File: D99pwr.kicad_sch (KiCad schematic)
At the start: 40 parts, among them IC1 TPS560430YFQDBVRQ1, IC2 NCP730BMT1500TBG, Q3B BC847BDW1, U2 MAX40203AUK, U3 MCP1640BCH, U4 MAX40203AUK

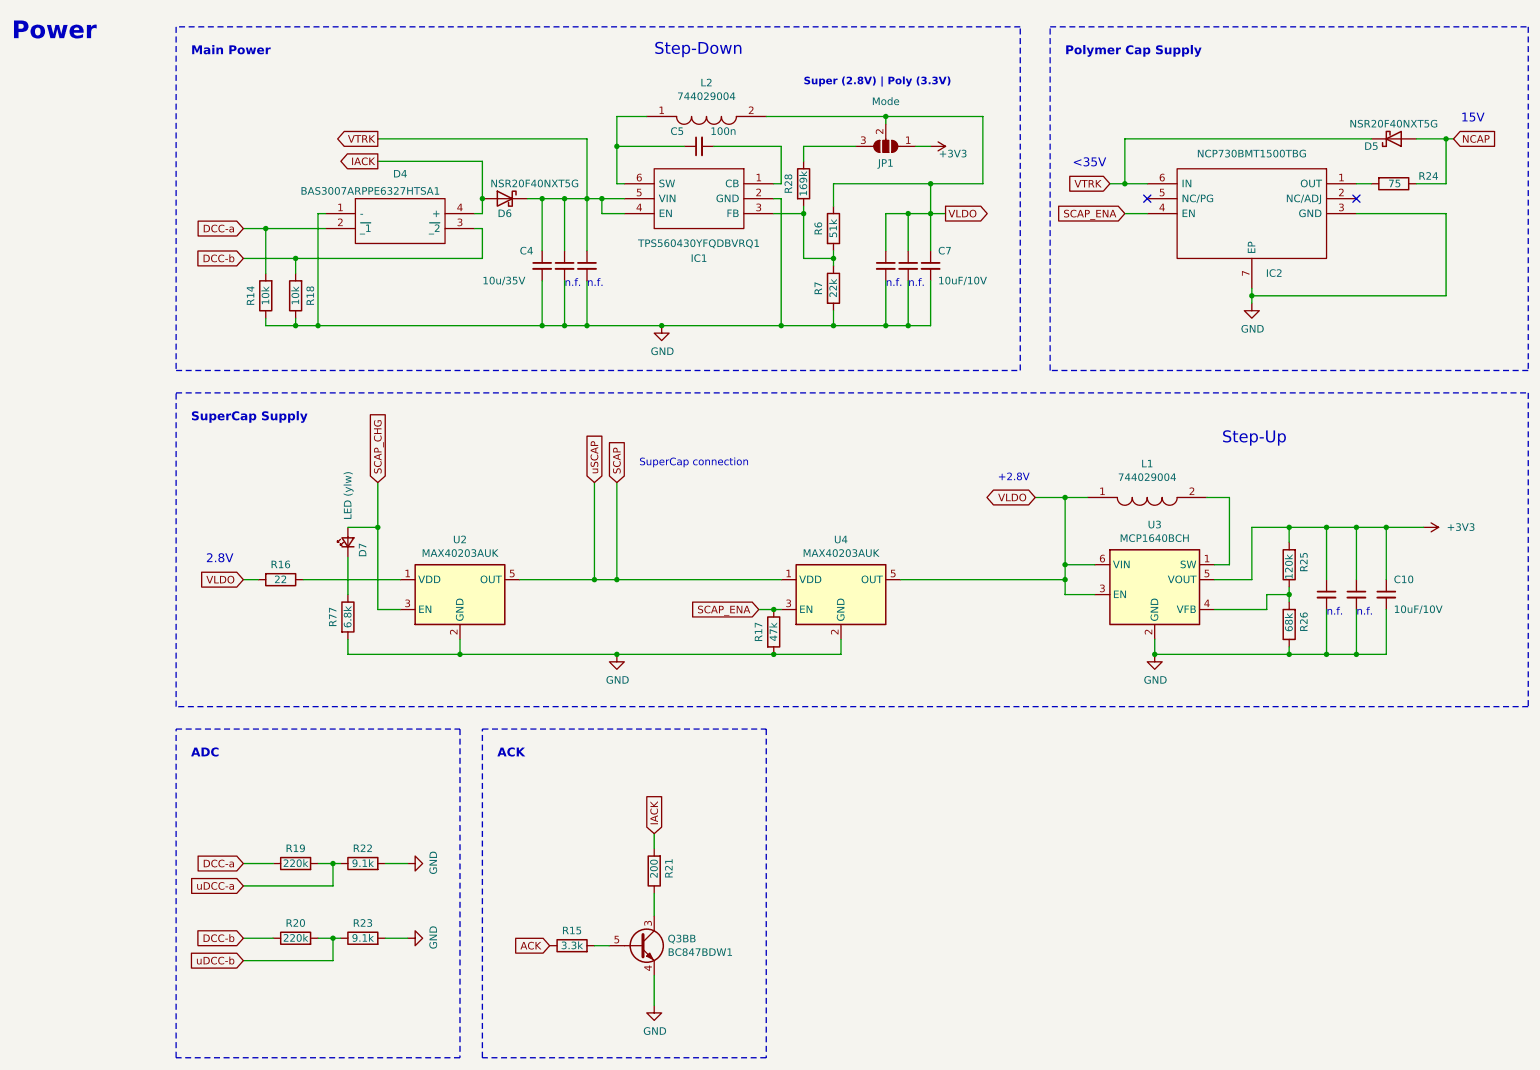
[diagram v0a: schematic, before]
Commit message: mod: ncap leakage resistor
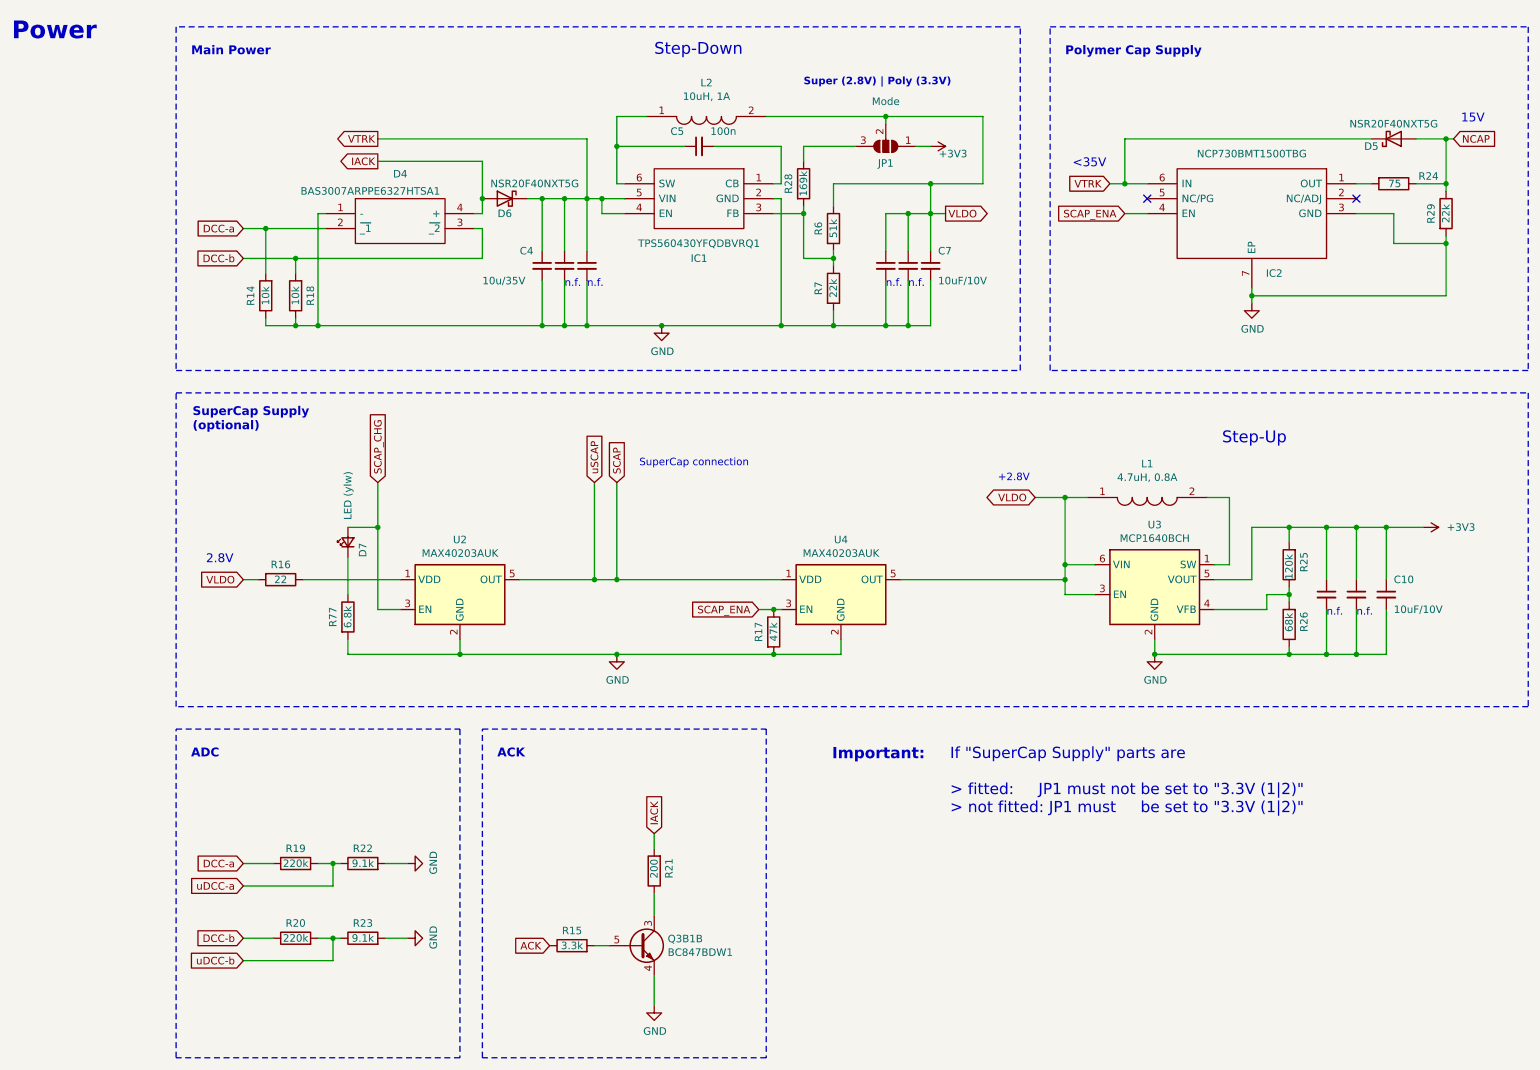
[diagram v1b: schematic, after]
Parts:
- added R29: 22k, Resistor_SMD:R_0402_1005Metric, symbol Device:R
- D5, D6: footprint Diode_SMD:D_0603_1608Metric -> RTB:NSR20F40NXT5G
- L1: value 744029004 -> 4.7uH, 0.8A
- L2: value 744029004 -> 10uH, 1A; JLCPCB C2649333 -> C2045611
- renumbered Q3B to Q3B1
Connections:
- net GND: now also R29.2
- net NCAP: now also R29.1
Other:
- note added: "If "SuperCap Supply" parts are > fitted: JP1 must not be set to "3.3V (1|2)" > not fitted: JP1 must be set to "3.3V (1|2)""
- note added: "Important:"
- note added: "SuperCap Supply (optional)"
- note removed: "SuperCap Supply"
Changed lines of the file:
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@@
 		)
 	)
+	(text "If \"SuperCap Supply\" parts are\n\n> fitted:     JP1 must not be set to \"3.3V (1|2)\"\n> not fitted: JP1 must     be set to \"3.3V (1|2)\""
+		(exclude_from_sim no)
+		(at 176.022 144.78 0)
+		(effects
+			(font
+				(size 1.905 1.905)
+				(thickness 0.2381)
+				(color 0 0 0 1)
+			)
+			(justify left)
+		)
+	)
 	(text "n.f."
 		(exclude_from_sim no)
@@
 		)
 	)
-	(text "SuperCap Supply"
+	(text "SuperCap Supply\n(optional)"
 		(exclude_from_sim no)
-		(at 46.99 83.82 0)
+		(at 47.244 85.344 0)
 		(effects
 			(font
@@
 		)
 	)
+	(text "Important:"
+		(exclude_from_sim no)
+		(at 155.956 140.208 0)
+		(effects
+			(font
+				(size 1.905 1.905)
+				(thickness 0.381)
+				(bold yes)
+				(color 194 0 194 1)
+			)
+			(justify left)
+		)
+	)
 	(text "15V"
 		(exclude_from_sim no)
@@
 	)
 	(junction
+		(at 260.35 53.34)
+		(diameter 0)
+		(color 0 0 0 0)
+	)
+	(junction
 		(at 233.68 101.6)
 		(diameter 0)
@@
 	)
 	(junction
+		(at 260.35 43.18)
+		(diameter 0)
+		(color 0 0 0 0)
+	)
+	(junction
 		(at 64.77 67.31)
 		(diameter 0)
@@
 	(wire
 		(pts
+			(xy 260.35 52.07) (xy 260.35 53.34)
+		)
+		(stroke
+			(width 0)
+			(type default)
+		)
+	)
+	(wire
+		(pts
 			(xy 106.68 54.61) (xy 106.68 45.72)
 		)
@@
 	(wire
 		(pts
-			(xy 260.35 48.26) (xy 260.35 62.23)
+			(xy 260.35 53.34) (xy 260.35 62.23)
 		)
 		(stroke
@@
 	(wire
 		(pts
+			(xy 251.46 48.26) (xy 245.11 48.26)
+		)
+		(stroke
+			(width 0)
+			(type default)
+		)
+	)
+	(wire
+		(pts
 			(xy 260.35 35.56) (xy 261.62 35.56)
 		)
@@
 	(wire
 		(pts
+			(xy 251.46 53.34) (xy 251.46 48.26)
+		)
+		(stroke
+			(width 0)
+			(type default)
+		)
+	)
+	(wire
+		(pts
 			(xy 78.74 101.6) (xy 78.74 93.98)
 		)
@@
 	(wire
 		(pts
-			(xy 245.11 48.26) (xy 260.35 48.26)
+			(xy 251.46 53.34) (xy 260.35 53.34)
 		)
 		(stroke
@@
 	(wire
 		(pts
+			(xy 260.35 43.18) (xy 260.35 44.45)
+		)
+		(stroke
+			(width 0)
+			(type default)
+		)
+	)
+	(wire
+		(pts
 			(xy 156.21 43.18) (xy 172.72 43.18)
 		)
@@
 		(on_board yes)
 		(dnp no)
-		(property "Reference" "Q3B"
+		(property "Reference" "Q3B1"
 			(at 128.016 171.5516 0)
 			(effects
@@
 			(project "D99"
 				(path "/df79ce8b-a870-46f6-824c-d442122538ae/00000000-0000-0000-0000-00005ca7768a"
-					(reference "Q3B")
+					(reference "Q3B1")
 					(unit 2)
 				)
@@
 			)
 		)
-		(property "Footprint" "Diode_SMD:D_0603_1608Metric"
+		(property "Footprint" "RTB:NSR20F40NXT5G"
 			(at 100.33 45.72 0)
 			(effects
@@
 			)
 		)
-		(property "Footprint" "Diode_SMD:D_0603_1608Metric"
+		(property "Footprint" "RTB:NSR20F40NXT5G"
 			(at 251.46 35.56 0)
 			(effects
@@
 			)
 		)
-		(property "Value" "744029004"
+		(property "Value" "4.7uH, 0.8A"
 			(at 209.55 93.1164 0)
 			(effects
@@
 			)
 		)
-		(property "Value" "744029004"
+		(property "Value" "10uH, 1A"
 			(at 134.62 28.3464 0)
 			(effects
@@
 			)
 		)
-		(property "Datasheet" "http://componentsearchengine.com/Datasheets/1/744029004.pdf"
+		(property "Datasheet" "http://componentsearchengine.com/Datasheets/1/744025100.pdf"
 			(at 140.97 33.02 0)
 			(effects
@@
 			)
 		)
-		(property "Description" "170mΩ 4.7uH 800mA 800mA ±30% SMD,2.8x2.8mm Power Inductors ROHS"
+		(property "Description" "1.1A 10uH 190mΩ 1A ±20% 2828 Power Inductors ROHS"
 			(at 140.97 35.56 0)
 			(effects
@@
 			)
 		)
-		(property "JLCPCB" "C2649333"
+		(property "JLCPCB" "C2045611"
 			(at 124.46 31.75 0)
 			(effects
@@
 					(unit 1)
 				)
+			)
+		)
+	)
+	(symbol
+		(lib_id "Device:R")
+		(at 260.35 48.26 0)
+		(unit 1)
+		(exclude_from_sim no)
+		(in_bom yes)
+		(on_board yes)
+		(dnp no)
+		(property "Reference" "R29"
+			(at 257.81 48.26 90)
+			(effects
+				(font
+					(size 1.27 1.27)
+				)
+			)
+		)
+		(property "Value" "22k"
+			(at 260.35 48.26 90)
+			(effects
+				(font
+					(size 1.27 1.27)
+				)
+			)
+		)
+		(property "Footprint" "Resistor_SMD:R_0402_1005Metric"
+			(at 258.572 48.26 90)
+			(effects
+				(font
+					(size 1.27 1.27)
+				)
+				(hide yes)
+			)
+		)
+		(property "Datasheet" "~"
+			(at 260.35 48.26 0)
+			(effects
+				(font
+					(size 1.27 1.27)
+				)
+				(hide yes)
+			)
+		)
+		(property "Description" ""
+			(at 260.35 48.26 90)
+			(effects
+				(font
+					(size 1.27 1.27)
+				)
+				(hide yes)
+			)
+		)
+		(property "JLCPCB" ""
+			(at 260.35 48.26 90)
+			(effects
+				(font
+					(size 1.27 1.27)
+				)
+				(hide yes)
+			)
+		)
+		(pin "1"
+		)
+		(pin "2"
+		)
+		(instances
+			(project "D99"
+				(path "/df79ce8b-a870-46f6-824c-d442122538ae/00000000-0000-0000-0000-00005ca7768a"
+					(reference "R29")
+					(unit 1)
+				)

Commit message: mod: refactoring
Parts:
- C10, C11, C6, C7, C8, C9: JLCPCB C19702 -> (none); LCSC Part # (none) -> C19702
- C12, C13, C4: JLCPCB C194427 -> (none); LCSC Part # (none) -> C194427
- C5: JLCPCB C307331 -> (none); LCSC Part # (none) -> C307331
- D4: JLCPCB C6430958 -> (none); LCSC Part # (none) -> C6430958
- D5, D6: JLCPCB C153761 -> (none); LCSC Part # (none) -> C153761
- IC1: JLCPCB C1849549 -> (none); LCSC Part # (none) -> C1849549
- IC2: JLCPCB C892817 -> (none); LCSC Part # (none) -> C892817
- L1: JLCPCB C2649333 -> (none); LCSC Part # (none) -> C2649333
- L2: JLCPCB C2045611 -> (none); LCSC Part # (none) -> C2045611
- Q3B1: JLCPCB C82368 -> (none); LCSC Part # (none) -> C82368
- R14, R18: JLCPCB C25744 -> (none); LCSC Part # (none) -> C25744
- R15: JLCPCB C25890 -> (none); LCSC Part # (none) -> C25890
- R16: JLCPCB C25092 -> (none); LCSC Part # (none) -> C25092
- R17: JLCPCB C25792 -> (none); LCSC Part # (none) -> C25792
- R19, R20: JLCPCB C25767 -> (none); LCSC Part # (none) -> C25767
- R21: JLCPCB C8218 -> (none); LCSC Part # (none) -> C8218
- R22, R23: JLCPCB C25926 -> (none); LCSC Part # (none) -> C25926
- R24: JLCPCB C4275 -> (none); LCSC Part # (none) -> C4275
- R25: JLCPCB C25750 -> (none); LCSC Part # (none) -> C25750
- R26: JLCPCB C36871 -> (none); LCSC Part # (none) -> C36871
- R28: JLCPCB C25758 -> (none); LCSC Part # (none) -> C25758
- R29: LCSC Part # (none) -> C25768
- R6: JLCPCB C25794 -> (none); LCSC Part # (none) -> C25794
- R7: JLCPCB C25768 -> (none); LCSC Part # (none) -> C25768
- R77: JLCPCB C23212 -> (none); LCSC Part # (none) -> C23212
- U2: LCSC Part # (none) -> C2653639
- U3: JLCPCB C478087 -> (none); LCSC Part # (none) -> C478087
- U4: JLCPCB C2653639 -> (none); LCSC Part # (none) -> C2653639
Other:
- note added: "3.3V: R25 = 120 Ohm 5.1V: R25 = 220 Ohm Use 1% Resistors for R25,R26"
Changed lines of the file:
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@@
 		)
 	)
+	(text "3.3V: R25 = 120 Ohm\n5.1V: R25 = 220 Ohm\nUse 1% Resistors for R25,R26"
+		(exclude_from_sim no)
+		(at 228.092 95.25 0)
+		(effects
+			(font
+				(size 1.27 1.27)
+			)
+			(justify left)
+		)
+	)
 	(text "Main Power"
 		(exclude_from_sim no)
@@
 			)
 		)
-		(property "JLCPCB" "C19702"
+		(property "LCSC Part #" "C19702"
 			(at 245.11 113.03 0)
 			(effects
@@
 			)
 		)
-		(property "JLCPCB" "C8218"
+		(property "LCSC Part #" "C8218"
 			(at 125.73 160.02 90)
 			(effects
@@
 			)
 		)
-		(property "JLCPCB" "C25890"
+		(property "LCSC Part #" "C25890"
 			(at 111.76 172.72 90)
 			(effects
@@
 			)
 		)
-		(property "JLCPCB" "C19702"
+		(property "LCSC Part #" "C19702"
 			(at 172.72 57.15 0)
 			(effects
@@
 			)
 		)
-		(property "JLCPCB" "C82368"
+		(property "LCSC Part #" "C82368"
 			(at 123.19 172.72 0)
 			(effects
@@
 			)
 		)
-		(property "JLCPCB" "C25767"
+		(property "LCSC Part #" "C25767"
 			(at 64.77 158.75 90)
 			(effects
@@
 			)
 		)
-		(property "JLCPCB" "C25926"
+		(property "LCSC Part #" "C25926"
 			(at 76.2 158.75 90)
 			(effects
@@
 			)
 		)
-		(property "JLCPCB" "C25767"
+		(property "LCSC Part #" "C25767"
 			(at 64.77 171.45 90)
 			(effects
@@
 			)
 		)
-		(property "JLCPCB" "C25926"
+		(property "LCSC Part #" "C25926"
 			(at 76.2 171.45 90)
 			(effects
@@
 			)
 		)
-		(property "JLCPCB" "C2653639"
+		(property "LCSC Part #" "C2653639"
 			(at 157.48 113.03 0)
 			(effects
@@
 			)
 		)
-		(property "JLCPCB" "C25750"
+		(property "LCSC Part #" "C25750"
 			(at 233.68 107.95 90)
 			(effects
@@
 			)
 		)
-		(property "JLCPCB" "C36871"
+		(property "LCSC Part #" "C36871"
 			(at 233.68 118.11 90)
 			(effects
@@
 			)
 		)
-		(property "JLCPCB" "C25744"
+		(property "LCSC Part #" "C25744"
 			(at 64.77 62.23 90)
 			(effects
@@
 			)
 		)
-		(property "JLCPCB" "C478087"
+		(property "LCSC Part #" "C478087"
 			(at 210.82 113.03 0)
 			(effects
@@
 			)
 		)
-		(property "JLCPCB" "C23212"
+		(property "LCSC Part #" "C23212"
 			(at 73.66 116.84 90)
 			(effects
@@
 			)
 		)
-		(property "JLCPCB" "C25744"
+		(property "LCSC Part #" "C25744"
 			(at 59.69 62.23 90)
 			(effects
@@
 			)
 		)
-		(property "JLCPCB" "C194427"
+		(property "LCSC Part #" "C194427"
 			(at 106.68 57.15 0)
 			(effects
@@
 			)
 		)
-		(property "JLCPCB" "C25092"
+		(property "LCSC Part #" "C25092"
 			(at 62.23 110.49 90)
 			(effects
@@
 			)
 		)
-		(property "JLCPCB" ""
+		(property "LCSC Part #" "C2653639"
 			(at 92.71 113.03 0)
 			(effects
@@
 			)
 		)
-		(property "JLCPCB" "C25792"
+		(property "LCSC Part #" "C25792"
 			(at 146.05 119.38 90)
 			(effects
@@
 			)
 		)
-		(property "JLCPCB" "C6430958"
+		(property "LCSC Part #" "C6430958"
 			(at 69.85 48.26 0)
 			(effects
@@
 			)
 		)
-		(property "JLCPCB" "C1849549"
+		(property "LCSC Part #" "C1849549"
 			(at 146.05 43.18 0)
 			(effects
@@
 			)
 		)
-		(property "JLCPCB" "C307331"
+		(property "LCSC Part #" "C307331"
 			(at 133.35 36.83 90)
 			(effects
@@
 			)
 		)
-		(property "JLCPCB" "C19702"
+		(property "LCSC Part #" "C19702"
 			(at 250.19 113.03 0)
 			(effects
@@
 			)
 		)
-		(property "JLCPCB" "C19702"
+		(property "LCSC Part #" "C19702"
 			(at 168.91 57.15 0)
 			(effects
@@
 			)
 		)
-		(property "JLCPCB" "C153761"
+		(property "LCSC Part #" "C153761"
 			(at 100.33 45.72 0)
 			(effects
@@
 			)
 		)
-		(property "JLCPCB" "C153761"
+		(property "LCSC Part #" "C153761"
 			(at 251.46 35.56 0)
 			(effects
@@
 			)
 		)
-		(property "JLCPCB" "C4275"
+		(property "LCSC Part #" "C4275"
 			(at 251.46 43.18 90)
 			(effects
@@
 			)
 		)
-		(property "JLCPCB" "C19702"
+		(property "LCSC Part #" "C19702"
 			(at 165.1 57.15 0)
 			(effects
@@
 			)
 		)
-		(property "JLCPCB" "C2649333"
+		(property "LCSC Part #" "C2649333"
 			(at 199.39 96.52 0)
 			(effects
@@
 			)
 		)
-		(property "JLCPCB" "C2045611"
+		(property "LCSC Part #" "C2045611"
 			(at 124.46 31.75 0)
 			(effects
@@
 			)
 		)
-		(property "JLCPCB" "C19702"
+		(property "LCSC Part #" "C19702"
 			(at 240.03 113.03 0)
 			(effects
@@
 			)
 		)
-		(property "JLCPCB" "C194427"
+		(property "LCSC Part #" "C194427"
 			(at 110.49 57.15 0)
 			(effects
@@
 			)
 		)
-		(property "JLCPCB" "C194427"
+		(property "LCSC Part #" "C194427"
 			(at 114.3 57.15 0)
 			(effects
@@
 			)
 		)
-		(property "JLCPCB" "C25794"
+		(property "LCSC Part #" "C25794"
 			(at 156.21 50.8 90)
 			(effects
@@
 			)
 		)
-		(property "JLCPCB" "C25768"
+		(property "LCSC Part #" "C25768"
 			(at 156.21 60.96 90)
 			(effects
@@
 			)
 		)
-		(property "JLCPCB" "C25758"
+		(property "LCSC Part #" "C25758"
 			(at 151.13 43.18 90)
 			(effects
@@
 			)
 		)
-		(property "JLCPCB" "C892817"
+		(property "LCSC Part #" "C892817"
 			(at 245.11 43.18 0)
 			(effects
@@
 			)
 		)
-		(property "Description" ""
+		(property "Description" "-55℃~+155℃ 22kΩ 50V 62.5mW Thick Film Resistor ±1% ±100ppm/℃ 0402 Chip Resistor - Surface Mount ROHS"
 			(at 260.35 48.26 90)
 			(effects
@@
 			)
 		)
-		(property "JLCPCB" ""
+		(property "LCSC Part #" "C25768"
 			(at 260.35 48.26 90)
 			(effects

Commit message: mod: refactoring
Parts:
- added unit 1 of Q3
- R21: value 200 -> 150; LCSC Part # C8218 -> C22808
- renumbered Q3B1 to Q3
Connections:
- no-connect marks 2 -> 5
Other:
- note added: "(or 5.0V)"
- note added: "3.3V: R25 = 120 Ohm 5.0V: R25 = 210 Ohm Use 1% Resistors for R25,R26"
- note removed: "3.3V: R25 = 120 Ohm 5.1V: R25 = 220 Ohm Use 1% Resistors for R25,R26"
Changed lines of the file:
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@@
 		)
 	)
+	(text "(or 5.0V)"
+		(exclude_from_sim no)
+		(at 264.668 104.394 0)
+		(effects
+			(font
+				(size 1.27 1.27)
+			)
+		)
+	)
 	(text "ACK"
 		(exclude_from_sim no)
@@
 		)
 	)
-	(text "3.3V: R25 = 120 Ohm\n5.1V: R25 = 220 Ohm\nUse 1% Resistors for R25,R26"
+	(text "3.3V: R25 = 120 Ohm\n5.0V: R25 = 210 Ohm\nUse 1% Resistors for R25,R26"
 		(exclude_from_sim no)
 		(at 228.092 95.25 0)
@@
 	)
 	(no_connect
+		(at 100.33 151.13)
+	)
+	(no_connect
+		(at 107.95 156.21)
+	)
+	(no_connect
 		(at 245.11 45.72)
 	)
+	(no_connect
+		(at 107.95 146.05)
+	)
 	(polyline
 		(pts
@@
 			)
 		)
-		(property "Value" "200"
+		(property "Value" "150"
 			(at 125.73 161.29 90)
 			(effects
@@
 			)
 		)
-		(property "Description" "-55℃~+155℃ 100mW 200Ω 75V Thick Film Resistor ±1% ±100ppm/℃ 0603 Chip Resistor - Surface Mount ROHS"
+		(property "Description" "-55℃~+155℃ 100mW 150Ω 75V Thick Film Resistor ±1% ±100ppm/℃ 0603 Chip Resistor - Surface Mount ROHS"
 			(at 125.73 160.02 90)
 			(effects
@@
 			)
 		)
-		(property "LCSC Part #" "C8218"
+		(property "LCSC Part #" "C22808"
 			(at 125.73 160.02 90)
 			(effects
@@
 		(on_board yes)
 		(dnp no)
-		(property "Reference" "Q3B1"
+		(property "Reference" "Q3"
 			(at 128.016 171.5516 0)
 			(effects
@@
 			(project "D99"
 				(path "/df79ce8b-a870-46f6-824c-d442122538ae/00000000-0000-0000-0000-00005ca7768a"
-					(reference "Q3B1")
+					(reference "Q3")
 					(unit 2)
 				)
@@
 					(unit 1)
 				)
+			)
+		)
+	)
+	(symbol
+		(lib_id "Transistor_BJT:BC847BDW1")
+		(at 105.41 151.13 0)
+		(unit 1)
+		(exclude_from_sim no)
+		(in_bom yes)
+		(on_board yes)
+		(dnp no)
+		(property "Reference" "Q3"
+			(at 110.236 149.9616 0)
+			(effects
+				(font
+					(size 1.27 1.27)
+				)
+				(justify left)
+			)
+		)
+		(property "Value" "BC847BDW1"
+			(at 110.236 152.273 0)
+			(effects
+				(font
+					(size 1.27 1.27)
+				)
+				(justify left)
+				(hide yes)
+			)
+		)
+		(property "Footprint" "Package_TO_SOT_SMD:SOT-363_SC-70-6"
+			(at 110.49 148.59 0)
+			(effects
+				(font
+					(size 1.27 1.27)
+				)
+				(hide yes)
+			)
+		)
+		(property "Datasheet" "http://www.onsemi.com/pub_link/Collateral/BC846BDW1T1-D.PDF"
+			(at 105.41 151.13 0)
+			(effects
+				(font
+					(size 1.27 1.27)
+				)
+				(hide yes)
+			)
+		)
+		(property "Description" "-55℃~+150℃ 100MHz 100mA 150@10uA,5.0V 250mV 380mW 45V 5uA NPN SOT-363 Bipolar (BJT) ROHS"
+			(at 105.41 151.13 0)
+			(effects
+				(font
+					(size 1.27 1.27)
+				)
+				(hide yes)
+			)
+		)
+		(property "LCSC Part #" "C82368"
+			(at 105.41 151.13 0)
+			(effects
+				(font
+					(size 1.27 1.27)
+				)
+				(hide yes)
+			)
+		)
+		(pin "2"
+		)
+		(pin "1"
+		)
+		(pin "4"
+		)
+		(pin "6"
+		)
+		(pin "5"
+		)
+		(pin "3"
+		)
+		(instances
+			(project "D99"
+				(path "/df79ce8b-a870-46f6-824c-d442122538ae/00000000-0000-0000-0000-00005ca7768a"
+					(reference "Q3")
+					(unit 1)
+				)
